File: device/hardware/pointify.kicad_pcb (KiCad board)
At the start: 2 copper layers, 24.5 x 22.6 mm, 16 parts, among them J1 USB_C, J2 SWIO, J3 GND, J4 PWM1, J5 PWM2, U1 CH32X033F8P6

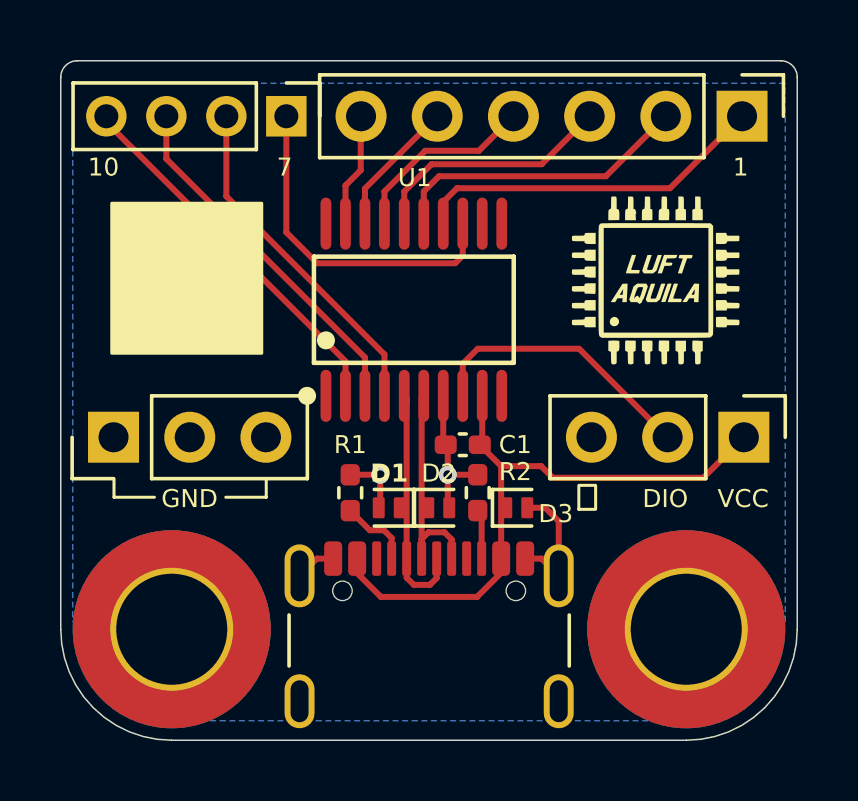
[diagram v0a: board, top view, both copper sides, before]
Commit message: pcb v2.1: fix pinmaps
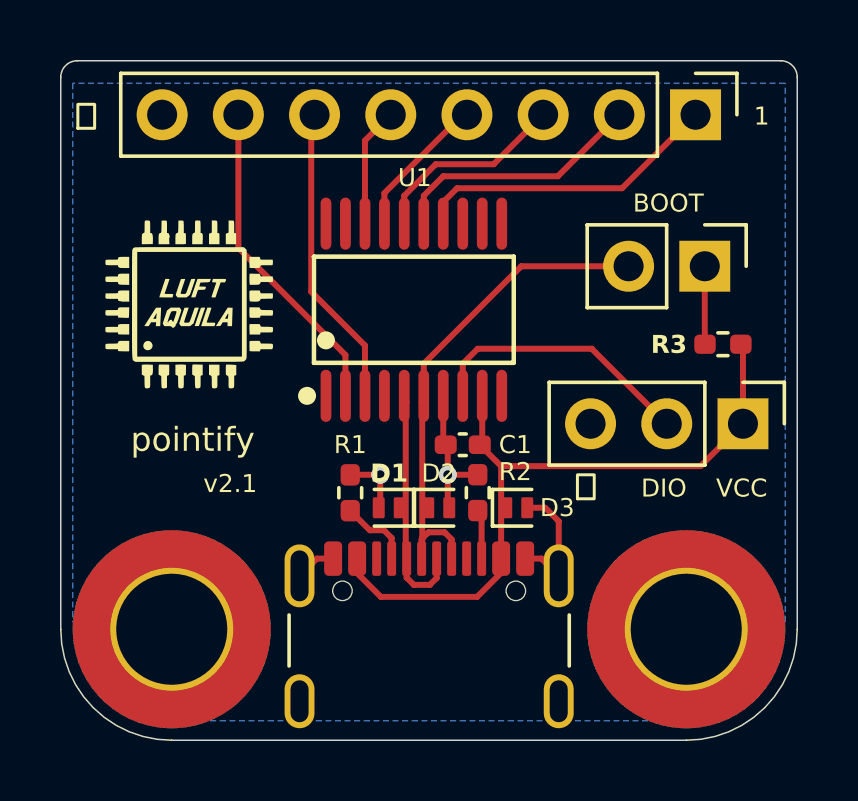
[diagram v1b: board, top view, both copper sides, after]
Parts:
- removed the J3 at (142.9, 110.5)
- removed J5: PWM2, Connector_PinHeader_2.00mm:PinHeader_1x04_P2.00mm_Vertical
- added JP1: BOOT, Connector_PinHeader_2.54mm:PinHeader_1x02_P2.54mm_Vertical, F.Cu at (162.6, 104.8)
- added R3: 1k, Resistor_SMD:R_0402_1005Metric_Pad0.72x0.64mm_HandSolder, F.Cu at (163.2, 107.3)
- J3: renamed from J4; value PWM1 -> PWM; footprint Connector_PinHeader_2.54mm:PinHeader_1x06_P2.54mm_Vertical -> Connector_PinHeader_2.54mm:PinHeader_1x08_P2.54mm_Vertical
- moved G*** 15.6 mm to (145.4, 106.0)
- moved J3 1.55 mm to (162.3, 99.7)
- moved G*** 1.35 mm to (153.4, 107.2)
- moved J2 0.45 mm to (163.9, 110.0)
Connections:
- net Net-(D1-A1) renamed /UDM
- net Net-(D2-A1) renamed /UDP
- J3 pad 6: /PWM6_T3C2 -> /PWM6_T1C3N
- U1 pad 13: /PWM7_T1C4 -> unconnected-(U1-PC3-Pad13)
- U1 pad 19: /PWM6_T3C2 -> unconnected-(U1-PA4-Pad19)
- U1 pad 2: /PWM10_T1C1N -> /PWM7_T1C1N
- U1 pad 3: /PWM9_T1C3N -> /PWM6_T1C3N
- U1 pad 4: /PWM8_T1C2N -> unconnected-(U1-PB7-Pad4)
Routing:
- net /PWM10_T1C1N: track 12.6 -> 0.00 mm
- net /PWM9_T1C3N: track 12.1 -> 0.00 mm
- net /PWM8_T1C2N: track 11.5 -> 0.00 mm
- net /PWM7_T1C4: track 11.4 -> 0.00 mm
- net /PWM7_T1C1N: track 0.00 -> 10.8 mm
- net /PWM6_T1C3N: track 0.00 -> 10.2 mm
- net /UDP: track 8.03 -> 17.3 mm
- net /PWM6_T3C2: track 3.80 -> 0.00 mm
- net Net-(JP1-A): track 0.00 -> 3.10 mm
- net +5V: track 21.2 -> 23.7 mm
- net /PWM3_T2C3: track 8.29 -> 6.68 mm
- net /PWM2_T2C2: track 10.2 -> 8.57 mm
- net /PWM4_T2C4: track 6.41 -> 4.85 mm
- net /PWM1_T2C1: track 11.9 -> 10.3 mm
- net /PWM5_T3C1: track 4.58 -> 3.99 mm
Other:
- board text added: "> --dangerously-skip-permissions"
- board text added: "BOOT"
- board text added: "pointify"
- board text added: "v2.1"
- board text added: "▐▛███▜▌ ▝▜█████▛▘ ▘▘ ▝▝"
- board text removed: "10"
- board text removed: "7"
- board text removed: "GND"

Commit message: update: translate font to polygons
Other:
- board text removed: "> --dangerously-skip-permissions"
- board text removed: "pointify"
- board text removed: "v2.1"
- board text removed: "▐▛███▜▌ ▝▜█████▛▘ ▘▘ ▝▝"

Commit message: update: pcb v2.2
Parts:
- removed D1, D2, D3: H5VL10B, Diode_SMD:D_SOD-882
- removed the J2 at (163.9, 110.0)
- added C2: 1uF, Capacitor_SMD:C_0402_1005Metric, F.Cu at (156.4, 113.0)
- C1: footprint Capacitor_SMD:C_0402_1005Metric_Pad0.74x0.62mm_HandSolder -> Capacitor_SMD:C_0402_1005Metric
- JP1: footprint Connector_PinHeader_2.54mm:PinHeader_1x02_P2.54mm_Vertical -> Connector_PinHeader_2.00mm:PinHeader_1x02_P2.00mm_Vertical
- R1, R2, R3: footprint Resistor_SMD:R_0402_1005Metric_Pad0.72x0.64mm_HandSolder -> Resistor_SMD:R_0402_1005Metric
- U1: footprint ch32x033f8p6:CH32X033F8P6 -> Package_SO:TSSOP-20_4.4x6.5mm_P0.65mm
- moved J2 17.9 mm to (144.5, 101.7), turned to 90 degrees
- moved R3 4.32 mm to (161.8, 111.5), turned to 90 degrees
- moved JP1 4.32 mm to (161.8, 109.0)
- moved G*** 1.72 mm to (145.7, 107.7)
- moved U1 1.49 mm to (152.9, 107.7), turned to 90 degrees
- moved C1 1.44 mm to (155.2, 112.0)
- moved G*** 1.40 mm to (153.4, 108.5)
- moved R2 0.82 mm to (154.6, 113.0), turned to 180 degrees
- moved R1 0.65 mm to (150.8, 113.0), turned to 180 degrees
- moved H1 0.55 mm to (145.4, 117.0)
- moved H2 0.54 mm to (161.5, 117.0)
- renumbered J3 to J2
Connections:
- J2 pad 1: /PWM1_T2C1 -> GND
- J2 pad 2: /PWM2_T2C2 -> /PWM1_T1C1N
- J2 pad 3: /PWM3_T2C3 -> /PWM2_T1C3N
- J2 pad 4: /PWM4_T2C4 -> /PWM3_T3C1
- J2 pad 5: /PWM5_T3C1 -> /PWM4_T2C4
- J2 pad 6: /PWM6_T1C3N -> /PWM5_T2C3
- J2 pad 7: /PWM7_T1C1N -> /PWM6_T2C2
- J2 pad 8: GND -> /PWM7_T2C1
- U1 pad 14: /PWM1_T2C1 -> /PWM7_T2C1
- U1 pad 15: /PWM2_T2C2 -> /PWM6_T2C2
- U1 pad 16: /PWM3_T2C3 -> /PWM5_T2C3
- U1 pad 18: /PWM5_T3C1 -> /PWM3_T3C1
- U1 pad 2: /PWM7_T1C1N -> /PWM1_T1C1N
- U1 pad 3: /PWM6_T1C3N -> /PWM2_T1C3N
- U1 pad 8: /DIO -> unconnected-(U1-PC18/DIO-Pad8)
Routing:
- net /PWM7_T1C1N: track 10.8 -> 0.00 mm
- net /PWM1_T1C1N: track 0.00 -> 10.4 mm
- net /PWM7_T2C1: track 0.00 -> 10.3 mm
- net /PWM1_T2C1: track 10.3 -> 0.00 mm
- net /PWM6_T1C3N: track 10.2 -> 0.00 mm
- net /PWM2_T1C3N: track 0.00 -> 10.0 mm
- net /DIO: track 9.11 -> 0.00 mm
- net /PWM2_T2C2: track 8.57 -> 0.00 mm
- net /PWM6_T2C2: track 0.00 -> 8.43 mm
- net /PWM3_T2C3: track 6.68 -> 0.00 mm
- net /PWM5_T2C3: track 0.00 -> 6.54 mm
- net +5V: track 23.7 -> 17.2 mm
- net /PWM5_T3C1: track 3.99 -> 0.00 mm
- net /PWM3_T3C1: track 0.00 -> 3.53 mm
- net /UDP: track 17.3 -> 14.2 mm
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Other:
- board size 24.5 x 22.6 mm -> 23.1 x 20.7 mm
- board text added: "7"
- board text added: "https://github.com/luftaquila/pointify"
- board text removed: "1"
- board text removed: "DIO"
- board text removed: "VCC"

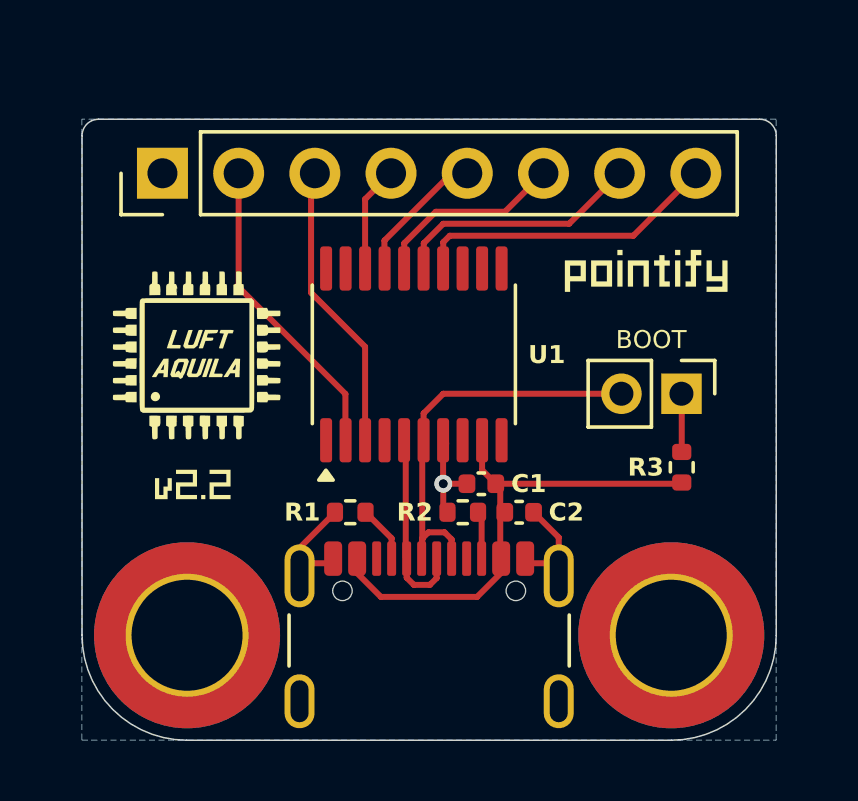
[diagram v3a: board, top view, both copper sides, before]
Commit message: update: pcb v2.3 with PWM8
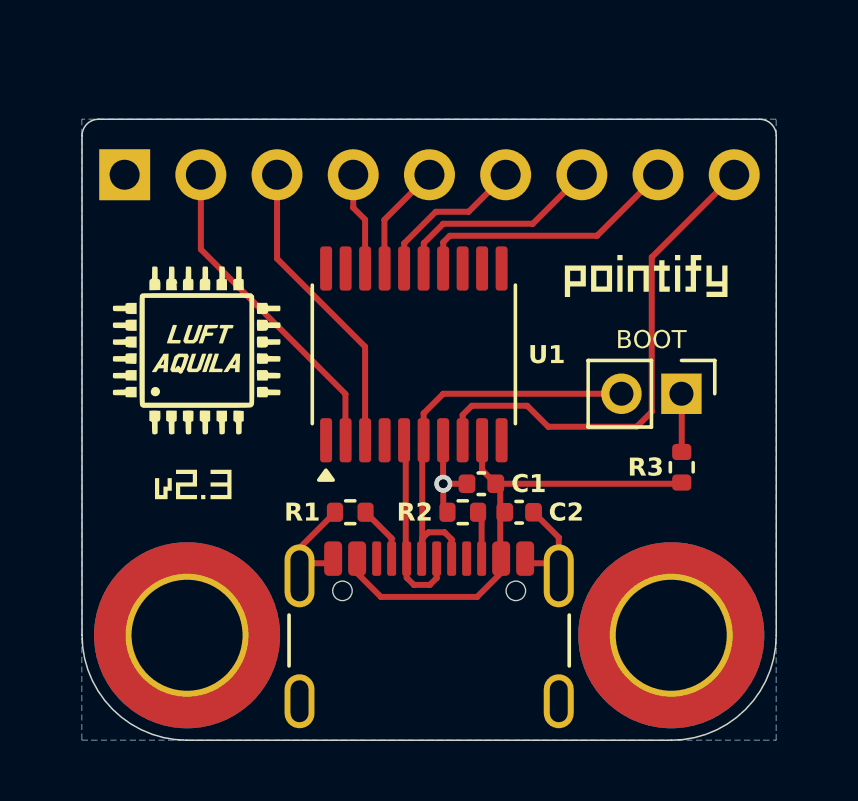
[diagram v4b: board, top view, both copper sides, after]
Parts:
- J2: footprint Connector_PinHeader_2.54mm:PinHeader_1x08_P2.54mm_Vertical -> Connector_PinHeader_2.54mm:PinHeader_1x09_P2.54mm_Vertical
- moved J2 1.26 mm to (143.3, 101.7)
- moved G*** 0.20 mm to (153.4, 108.8)
- moved G*** 0.17 mm to (145.7, 107.5)
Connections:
- U1 pad 8: unconnected-(U1-PC18/DIO-Pad8) -> /PWM8_T3C2
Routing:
- net /PWM8_T3C2: track 0.00 -> 16.8 mm
- net /PWM5_T2C3: track 6.54 -> 5.26 mm
- net /PWM7_T2C1: track 10.3 -> 9.06 mm
- net /PWM6_T2C2: track 8.43 -> 7.15 mm
- net /PWM4_T2C4: track 4.85 -> 3.91 mm
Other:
- board text added: "1"
- board text added: "2"
- board text added: "3"
- board text added: "4"
- board text added: "5"
- board text added: "6"
- board text added: "8"
